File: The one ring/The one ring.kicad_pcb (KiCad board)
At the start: 2 copper layers, 5 parts, among them J1 LiPo_100-150mAh, SW1 SW_Push, U1 XIAO-ESP32-S3-Sense, U2 MAX98357A

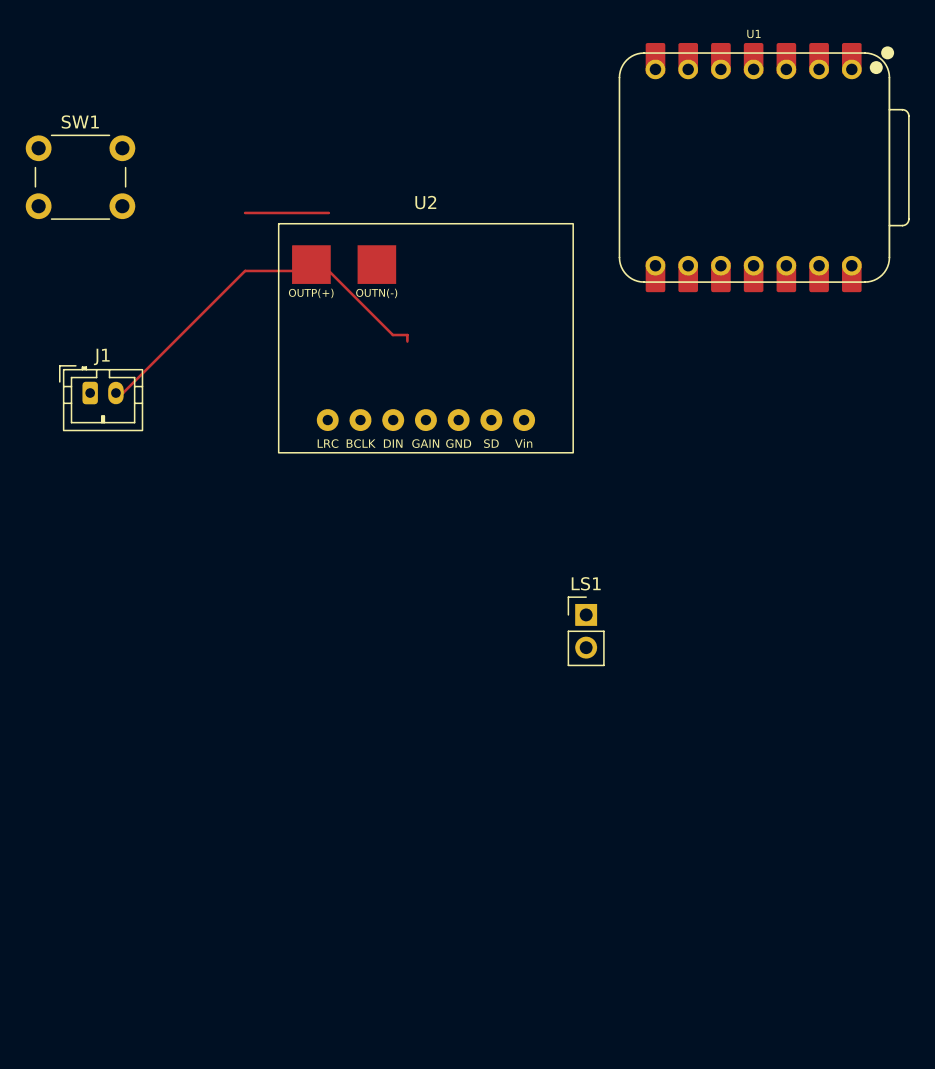
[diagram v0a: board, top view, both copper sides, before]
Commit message: Update gitignore and PCB footprint changes
Add .github_token to gitignore. Update PCB with custom MAX98357A breakout footprint.

Co-Authored-By: Claude Sonnet 4.6 <noreply@anthropic.com>
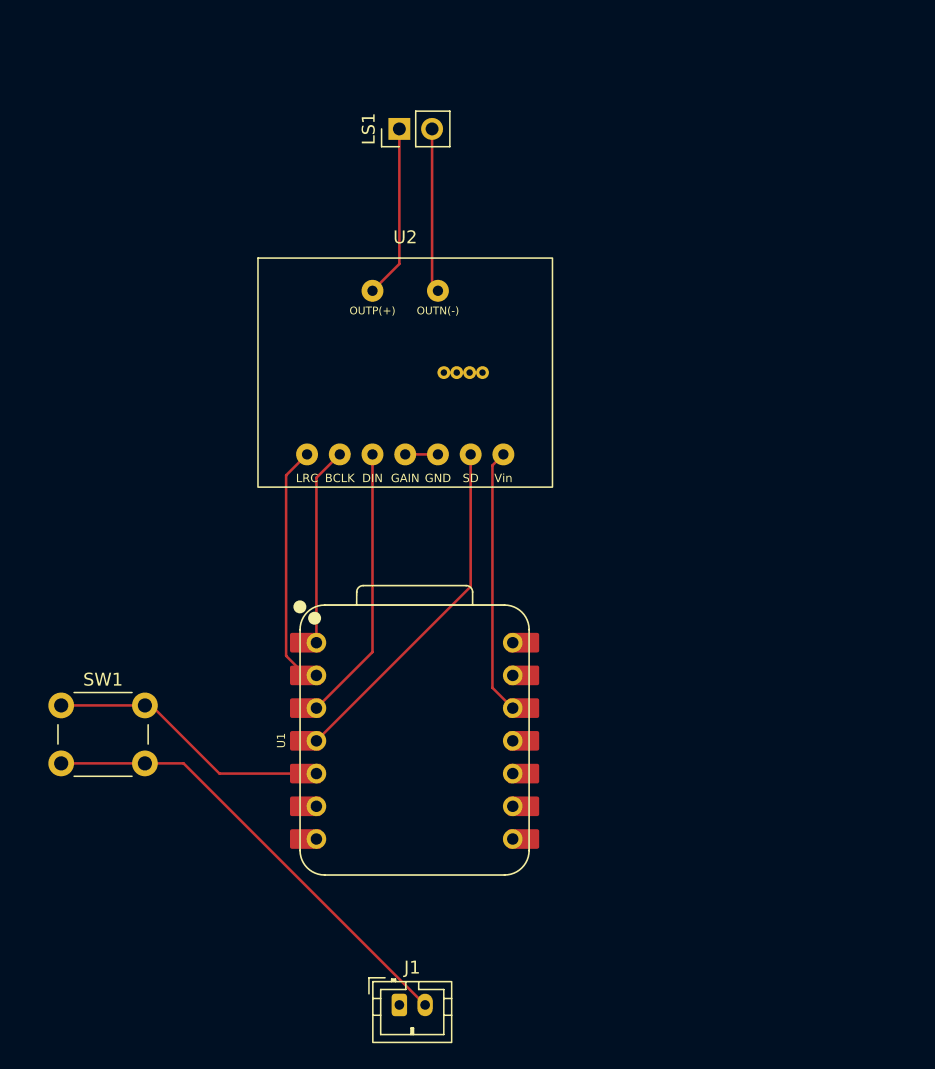
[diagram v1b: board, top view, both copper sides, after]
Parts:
- moved J1 53.2 mm to (126.5, 126.5)
- moved U1 51.7 mm to (127.7, 106.0), turned to 90 degrees
- moved SW1 43.3 mm to (100.2, 103.2)
- moved LS1 40.4 mm to (126.5, 58.5), turned to 90 degrees
- moved U2 3.11 mm to (127.0, 77.4)
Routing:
- net /AMP_SD: track 0.00 -> 27.2 mm
- net /I2S_DIN: track 0.00 -> 21.5 mm
- net +3.3V: track 0.00 -> 20.7 mm
- net /I2S_LRC: track 0.00 -> 18.5 mm
- net /I2S_BCLK: track 0.00 -> 15.4 mm
- net /BTN: track 6.50 -> 21.2 mm
- net /SPK_P: track 0.00 -> 13.4 mm
- net /SPK_N: track 0.00 -> 12.8 mm
- net GND: track 29.1 -> 38.6 mm

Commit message: Add +BATT note and update PCB footprints
Add schematic note documenting +BATT connects to XIAO onboard JST.
Update PCB with latest custom MAX98357A breakout footprint changes.

Co-Authored-By: Claude Sonnet 4.6 <noreply@anthropic.com>
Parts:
- moved J1 6.08 mm to (127.5, 120.5)
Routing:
- net GND: track 38.6 -> 28.6 mm
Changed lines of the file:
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@@
 	(footprint "Connector_JST:JST_PH_B2B-PH-K_1x02_P2.00mm_Vertical"
 		(layer "F.Cu")
-		(at 126.5 126.5)
+		(at 127.5 120.5)
 		(descr "JST PH series connector, B2B-PH-K (http://www.jst-mfg.com/product/pdf/eng/ePH.pdf)")
 		(tags "connector JST PH vertical")
@@
 	)
 	(segment
-		(start 109.75 107.75)
-		(end 128.5 126.5)
-		(width 0.2)
-		(layer "F.Cu")
-		(net "GND")
-	)
-	(segment
 		(start 100.25 107.75)
 		(end 106.75 107.75)
@@
 	)
 	(segment
-		(start 106.75 107.75)
-		(end 109.75 107.75)
-		(width 0.2)
-		(layer "F.Cu")
+		(start 129.495 95.1135)
+		(end 129.495 83.765)
+		(width 0.2)
+		(layer "B.Cu")
 		(net "GND")
+	)
+	(segment
+		(start 135.3015 100.92)
+		(end 129.495 95.1135)
+		(width 0.2)
+		(layer "B.Cu")
+		(net "GND")
+	)
+	(segment
+		(start 124.415 99.1065)
+		(end 120.0615 103.46)
+		(width 0.2)
+		(layer "F.Cu")
+		(net "/I2S_DIN")
+	)
+	(segment
+		(start 124.415 83.765)
+		(end 124.415 99.1065)
+		(width 0.2)
+		(layer "F.Cu")
+		(net "/I2S_DIN")
+	)
+	(segment
+		(start 132.035 83.765)
+		(end 132.035 94.0265)
+		(width 0.2)
+		(layer "F.Cu")
+		(net "/AMP_SD")
+	)
+	(segment
+		(start 132.035 94.0265)
+		(end 120.0615 106)
+		(width 0.2)
+		(layer "F.Cu")
+		(net "/AMP_SD")
+	)
+	(segment
+		(start 134.575 83.765)
+		(end 133.725 84.615)
+		(width 0.2)
+		(layer "F.Cu")
+		(net "+3.3V")
+	)
+	(segment
+		(start 133.725 84.615)
+		(end 133.725 101.8835)
+		(width 0.2)
+		(layer "F.Cu")
+		(net "+3.3V")
+	)
+	(segment
+		(start 133.725 101.8835)
+		(end 135.3015 103.46)
+		(width 0.2)
+		(layer "F.Cu")
+		(net "+3.3V")
 	)
 	(segment
@@
 	)
 	(segment
-		(start 124.415 99.1065)
-		(end 120.0615 103.46)
-		(width 0.2)
-		(layer "F.Cu")
-		(net "/I2S_DIN")
-	)
-	(segment
-		(start 124.415 83.765)
-		(end 124.415 99.1065)
-		(width 0.2)
-		(layer "F.Cu")
-		(net "/I2S_DIN")
-	)
-	(segment
-		(start 132.035 83.765)
-		(end 132.035 94.0265)
-		(width 0.2)
-		(layer "F.Cu")
-		(net "/AMP_SD")
-	)
-	(segment
-		(start 132.035 94.0265)
-		(end 120.0615 106)
-		(width 0.2)
-		(layer "F.Cu")
-		(net "/AMP_SD")
-	)
-	(segment
-		(start 134.575 83.765)
-		(end 133.725 84.615)
-		(width 0.2)
-		(layer "F.Cu")
-		(net "+3.3V")
-	)
-	(segment
-		(start 133.725 84.615)
-		(end 133.725 101.8835)
-		(width 0.2)
-		(layer "F.Cu")
-		(net "+3.3V")
-	)
-	(segment
-		(start 133.725 101.8835)
-		(end 135.3015 103.46)
-		(width 0.2)
-		(layer "F.Cu")
-		(net "+3.3V")
-	)
-	(segment
